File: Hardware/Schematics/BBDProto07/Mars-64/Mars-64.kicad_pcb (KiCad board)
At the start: 4 copper layers, 50.8 x 50.8 mm, 79 parts, among them J101 Conn_Coaxial, J102 Conn_Coaxial, U101 ADG731, U102 ADG731

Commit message: Created the rev D of the schematics
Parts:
- moved U102 72.1 mm to (78.7, 137.2)
- moved C2 71.1 mm to (61.0, 139.7), turned to 0 degrees
- moved J102 68.4 mm to (94.0, 137.2)
- moved JP5 58.8 mm to (61.0, 134.6), turned to 0 degrees
- moved H3 52.4 mm to (58.4, 127.0)
- moved H4 50.6 mm to (99.1, 127.0)
- moved TP109 49.1 mm to (61.0, 88.9)
- moved TP110 49.1 mm to (66.0, 88.9)
- moved TP111 49.1 mm to (71.1, 88.9)
- moved TP112 49.1 mm to (76.2, 88.9)
- moved TP113 49.1 mm to (81.3, 88.9)
- moved TP114 49.1 mm to (86.4, 88.9)
- moved TP115 49.1 mm to (91.4, 88.9)
- moved TP116 49.1 mm to (96.5, 88.9)
- moved TP117 49.1 mm to (61.0, 94.0)
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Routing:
- net GND: track 170.2 -> 0.00 mm, vias 2 -> 0
- net /VCC3V3: track 145.0 -> 0.00 mm
- net Net-(JP5-Pad2): track 112.4 -> 0.00 mm, vias 2 -> 0
- net /~SPI_CE: track 101.9 -> 0.00 mm, vias 3 -> 0
- net Net-(TP207-Pad1): track 74.5 -> 0.00 mm, vias 2 -> 1
- net Net-(J101-Pad2): track 70.3 -> 0.00 mm, vias 2 -> 0
- net Net-(TP217-Pad1): track 65.8 -> 0.00 mm, vias 2 -> 1
- net Net-(TP208-Pad1): track 64.1 -> 0.00 mm, vias 2 -> 1
- net /DB: track 56.3 -> 0.00 mm, vias 2 -> 0
- net Net-(TP123-Pad1): track 55.6 -> 0.00 mm, vias 2 -> 1
- net /DA: track 55.3 -> 0.00 mm, vias 2 -> 0
- net Net-(TP109-Pad1): track 53.6 -> 0.00 mm, vias 2 -> 1
- net Net-(TP111-Pad1): track 51.3 -> 0.00 mm, vias 2 -> 1
- net Net-(TP206-Pad1): track 51.2 -> 0.00 mm, vias 2 -> 1
- net Net-(TP220-Pad1): track 50.3 -> 0.00 mm, vias 2 -> 1
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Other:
- board size 50.8 x 50.8 mm -> 45.7 x 104.1 mm
- board text added: "BBD Mars-64 rev. D"
- board text removed: "BBD Mars-64 rev. C"

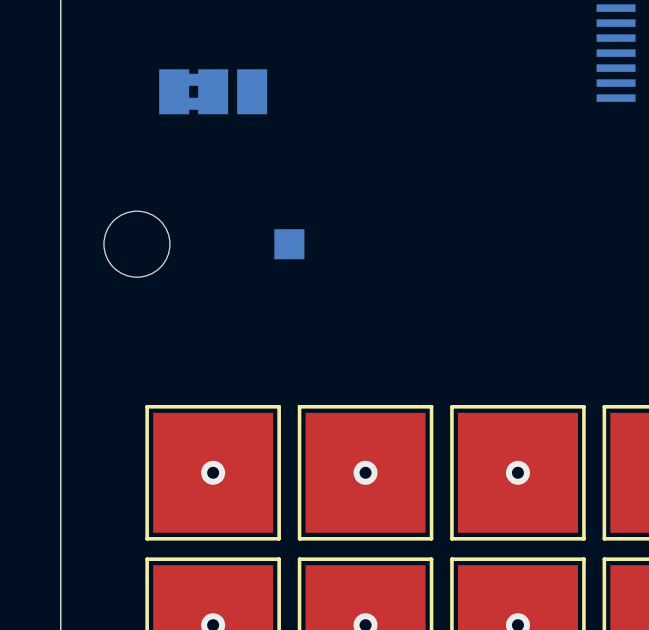
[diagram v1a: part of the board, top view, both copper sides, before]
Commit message: Connected the AGND to the fill zone
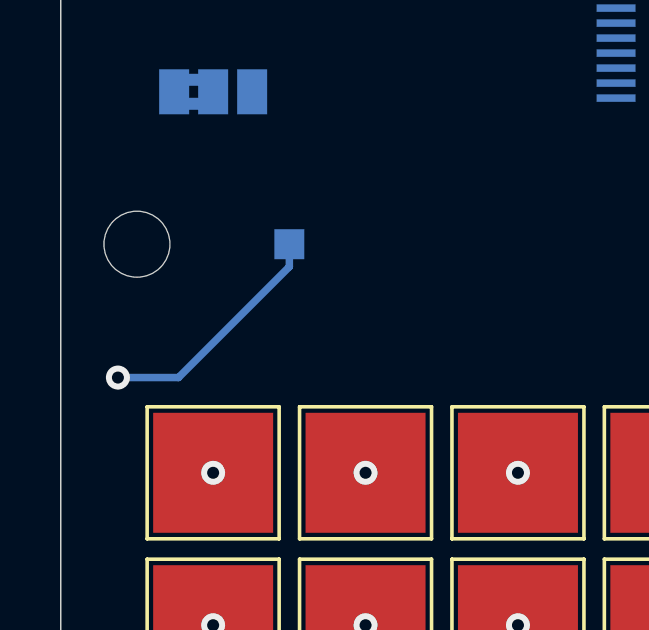
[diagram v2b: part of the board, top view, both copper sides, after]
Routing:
- net /AGND: track 0.00 -> 8.00 mm, vias 0 -> 1
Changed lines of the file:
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@@
     (thickness 1.6)
     (drawings 8)
-    (tracks 64)
+    (tracks 68)
     (zones 0)
     (modules 79)
@@
   (gr_line (start 101.6 144.78) (end 55.88 144.78) (layer Edge.Cuts) (width 0.05))
   (gr_line (start 55.88 40.64) (end 101.6 40.64) (layer Edge.Cuts) (width 0.05))
+  (via (at 57.785 80.645) (size 0.8) (drill 0.4) (layers F.Cu B.Cu) (net 6))
+  (segment (start 63.5 76.95) (end 63.5 76.2) (width 0.25) (layer B.Cu) (net 6))
+  (segment (start 59.805 80.645) (end 63.5 76.95) (width 0.25) (layer B.Cu) (net 6))
+  (segment (start 57.785 80.645) (end 59.805 80.645) (width 0.25) (layer B.Cu) (net 6))
+  (via (at 60.96 83.82) (size 0.8) (drill 0.4) (layers F.Cu B.Cu) (net 9))
+  (via (at 66.04 83.82) (size 0.8) (drill 0.4) (layers F.Cu B.Cu) (net 10))
+  (via (at 71.12 83.82) (size 0.8) (drill 0.4) (layers F.Cu B.Cu) (net 11))
+  (via (at 76.2 83.82) (size 0.8) (drill 0.4) (layers F.Cu B.Cu) (net 12))
+  (via (at 81.28 83.82) (size 0.8) (drill 0.4) (layers F.Cu B.Cu) (net 13))
+  (via (at 86.36 83.82) (size 0.8) (drill 0.4) (layers F.Cu B.Cu) (net 14))
+  (via (at 91.44 83.82) (size 0.8) (drill 0.4) (layers F.Cu B.Cu) (net 15))
+  (via (at 96.52 83.82) (size 0.8) (drill 0.4) (layers F.Cu B.Cu) (net 16))
+  (via (at 60.96 88.9) (size 0.8) (drill 0.4) (layers F.Cu B.Cu) (net 17))
+  (via (at 66.04 88.9) (size 0.8) (drill 0.4) (layers F.Cu B.Cu) (net 18))
+  (via (at 71.12 88.9) (size 0.8) (drill 0.4) (layers F.Cu B.Cu) (net 19))
+  (via (at 76.2 88.9) (size 0.8) (drill 0.4) (layers F.Cu B.Cu) (net 20))
+  (via (at 81.28 88.9) (size 0.8) (drill 0.4) (layers F.Cu B.Cu) (net 21))
+  (via (at 86.36 88.9) (size 0.8) (drill 0.4) (layers F.Cu B.Cu) (net 22))
+  (via (at 91.44 88.9) (size 0.8) (drill 0.4) (layers F.Cu B.Cu) (net 23))
+  (via (at 96.52 88.9) (size 0.8) (drill 0.4) (layers F.Cu B.Cu) (net 24))
+  (via (at 60.96 93.98) (size 0.8) (drill 0.4) (layers F.Cu B.Cu) (net 25))
+  (via (at 66.04 93.98) (size 0.8) (drill 0.4) (layers F.Cu B.Cu) (net 26))
+  (via (at 71.12 93.98) (size 0.8) (drill 0.4) (layers F.Cu B.Cu) (net 27))
+  (via (at 76.2 93.98) (size 0.8) (drill 0.4) (layers F.Cu B.Cu) (net 28))
+  (via (at 81.28 93.98) (size 0.8) (drill 0.4) (layers F.Cu B.Cu) (net 29))
+  (via (at 86.36 93.98) (size 0.8) (drill 0.4) (layers F.Cu B.Cu) (net 30))
+  (via (at 91.44 93.98) (size 0.8) (drill 0.4) (layers F.Cu B.Cu) (net 31))
+  (via (at 96.52 93.98) (size 0.8) (drill 0.4) (layers F.Cu B.Cu) (net 32))
+  (via (at 60.96 99.06) (size 0.8) (drill 0.4) (layers F.Cu B.Cu) (net 33))
+  (via (at 66.04 99.06) (size 0.8) (drill 0.4) (layers F.Cu B.Cu) (net 34))
+  (via (at 71.12 99.06) (size 0.8) (drill 0.4) (layers F.Cu B.Cu) (net 35))
+  (via (at 76.2 99.06) (size 0.8) (drill 0.4) (layers F.Cu B.Cu) (net 36))
+  (via (at 81.28 99.06) (size 0.8) (drill 0.4) (layers F.Cu B.Cu) (net 37))
+  (via (at 86.36 99.06) (size 0.8) (drill 0.4) (layers F.Cu B.Cu) (net 38))
+  (via (at 91.44 99.06) (size 0.8) (drill 0.4) (layers F.Cu B.Cu) (net 39))
+  (via (at 96.52 99.06) (size 0.8) (drill 0.4) (layers F.Cu B.Cu) (net 40))
+  (via (at 60.96 104.14) (size 0.8) (drill 0.4) (layers F.Cu B.Cu) (net 41))
+  (via (at 66.04 104.14) (size 0.8) (drill 0.4) (layers F.Cu B.Cu) (net 42))
+  (via (at 71.12 104.14) (size 0.8) (drill 0.4) (layers F.Cu B.Cu) (net 43))
+  (via (at 76.2 104.14) (size 0.8) (drill 0.4) (layers F.Cu B.Cu) (net 44))
+  (via (at 81.28 104.14) (size 0.8) (drill 0.4) (layers F.Cu B.Cu) (net 45))
+  (via (at 86.36 104.14) (size 0.8) (drill 0.4) (layers F.Cu B.Cu) (net 46))
+  (via (at 91.44 104.14) (size 0.8) (drill 0.4) (layers F.Cu B.Cu) (net 47))
+  (via (at 96.52 104.14) (size 0.8) (drill 0.4) (layers F.Cu B.Cu) (net 48))
+  (via (at 60.96 109.22) (size 0.8) (drill 0.4) (layers F.Cu B.Cu) (net 49))
+  (via (at 66.04 109.22) (size 0.8) (drill 0.4) (layers F.Cu B.Cu) (net 50))
+  (via (at 71.12 109.22) (size 0.8) (drill 0.4) (layers F.Cu B.Cu) (net 51))
+  (via (at 76.2 109.22) (size 0.8) (drill 0.4) (layers F.Cu B.Cu) (net 52))
+  (via (at 81.28 109.22) (size 0.8) (drill 0.4) (layers F.Cu B.Cu) (net 53))
+  (via (at 86.36 109.22) (size 0.8) (drill 0.4) (layers F.Cu B.Cu) (net 54))
+  (via (at 91.44 109.22) (size 0.8) (drill 0.4) (layers F.Cu B.Cu) (net 55))
+  (via (at 96.52 109.22) (size 0.8) (drill 0.4) (layers F.Cu B.Cu) (net 56))
+  (via (at 60.96 114.3) (size 0.8) (drill 0.4) (layers F.Cu B.Cu) (net 57))
+  (via (at 66.04 114.3) (size 0.8) (drill 0.4) (layers F.Cu B.Cu) (net 58))
+  (via (at 71.12 114.3) (size 0.8) (drill 0.4) (layers F.Cu B.Cu) (net 59))
+  (via (at 76.2 114.3) (size 0.8) (drill 0.4) (layers F.Cu B.Cu) (net 60))
+  (via (at 81.28 114.3) (size 0.8) (drill 0.4) (layers F.Cu B.Cu) (net 61))
+  (via (at 86.36 114.3) (size 0.8) (drill 0.4) (layers F.Cu B.Cu) (net 62))
+  (via (at 91.44 114.3) (size 0.8) (drill 0.4) (layers F.Cu B.Cu) (net 63))
+  (via (at 96.52 114.3) (size 0.8) (drill 0.4) (layers F.Cu B.Cu) (net 64))
   (via (at 60.96 119.38) (size 0.8) (drill 0.4) (layers F.Cu B.Cu) (net 65))
   (via (at 66.04 119.38) (size 0.8) (drill 0.4) (layers F.Cu B.Cu) (net 66))
@@
   (via (at 91.44 119.38) (size 0.8) (drill 0.4) (layers F.Cu B.Cu) (net 71))
   (via (at 96.52 119.38) (size 0.8) (drill 0.4) (layers F.Cu B.Cu) (net 72))
-  (via (at 96.52 114.3) (size 0.8) (drill 0.4) (layers F.Cu B.Cu) (net 64))
-  (via (at 91.44 114.3) (size 0.8) (drill 0.4) (layers F.Cu B.Cu) (net 63))
-  (via (at 86.36 114.3) (size 0.8) (drill 0.4) (layers F.Cu B.Cu) (net 62))
-  (via (at 81.28 114.3) (size 0.8) (drill 0.4) (layers F.Cu B.Cu) (net 61))
-  (via (at 76.2 114.3) (size 0.8) (drill 0.4) (layers F.Cu B.Cu) (net 60))
-  (via (at 71.12 114.3) (size 0.8) (drill 0.4) (layers F.Cu B.Cu) (net 59))
-  (via (at 66.04 114.3) (size 0.8) (drill 0.4) (layers F.Cu B.Cu) (net 58))
-  (via (at 60.96 114.3) (size 0.8) (drill 0.4) (layers F.Cu B.Cu) (net 57))
-  (via (at 60.96 109.22) (size 0.8) (drill 0.4) (layers F.Cu B.Cu) (net 49))
-  (via (at 66.04 109.22) (size 0.8) (drill 0.4) (layers F.Cu B.Cu) (net 50))
-  (via (at 71.12 109.22) (size 0.8) (drill 0.4) (layers F.Cu B.Cu) (net 51))
-  (via (at 76.2 109.22) (size 0.8) (drill 0.4) (layers F.Cu B.Cu) (net 52))
-  (via (at 81.28 109.22) (size 0.8) (drill 0.4) (layers F.Cu B.Cu) (net 53))
-  (via (at 86.36 109.22) (size 0.8) (drill 0.4) (layers F.Cu B.Cu) (net 54))
-  (via (at 91.44 109.22) (size 0.8) (drill 0.4) (layers F.Cu B.Cu) (net 55))
-  (via (at 96.52 109.22) (size 0.8) (drill 0.4) (layers F.Cu B.Cu) (net 56))
-  (via (at 96.52 104.14) (size 0.8) (drill 0.4) (layers F.Cu B.Cu) (net 48))
-  (via (at 91.44 104.14) (size 0.8) (drill 0.4) (layers F.Cu B.Cu) (net 47))
-  (via (at 86.36 104.14) (size 0.8) (drill 0.4) (layers F.Cu B.Cu) (net 46))
-  (via (at 81.28 104.14) (size 0.8) (drill 0.4) (layers F.Cu B.Cu) (net 45))
-  (via (at 76.2 104.14) (size 0.8) (drill 0.4) (layers F.Cu B.Cu) (net 44))
-  (via (at 71.12 104.14) (size 0.8) (drill 0.4) (layers F.Cu B.Cu) (net 43))
-  (via (at 66.04 104.14) (size 0.8) (drill 0.4) (layers F.Cu B.Cu) (net 42))
-  (via (at 60.96 104.14) (size 0.8) (drill 0.4) (layers F.Cu B.Cu) (net 41))
-  (via (at 60.96 93.98) (size 0.8) (drill 0.4) (layers F.Cu B.Cu) (net 25))
-  (via (at 60.96 99.06) (size 0.8) (drill 0.4) (layers F.Cu B.Cu) (net 33))
-  (via (at 66.04 99.06) (size 0.8) (drill 0.4) (layers F.Cu B.Cu) (net 34))
-  (via (at 66.04 93.98) (size 0.8) (drill 0.4) (layers F.Cu B.Cu) (net 26))
-  (via (at 96.52 99.06) (size 0.8) (drill 0.4) (layers F.Cu B.Cu) (net 40))
-  (via (at 91.44 99.06) (size 0.8) (drill 0.4) (layers F.Cu B.Cu) (net 39))
-  (via (at 86.36 99.06) (size 0.8) (drill 0.4) (layers F.Cu B.Cu) (net 38))
-  (via (at 81.28 99.06) (size 0.8) (drill 0.4) (layers F.Cu B.Cu) (net 37))
-  (via (at 76.2 99.06) (size 0.8) (drill 0.4) (layers F.Cu B.Cu) (net 36))
-  (via (at 71.12 99.06) (size 0.8) (drill 0.4) (layers F.Cu B.Cu) (net 35))
-  (via (at 71.12 93.98) (size 0.8) (drill 0.4) (layers F.Cu B.Cu) (net 27))
-  (via (at 76.2 93.98) (size 0.8) (drill 0.4) (layers F.Cu B.Cu) (net 28))
-  (via (at 81.28 93.98) (size 0.8) (drill 0.4) (layers F.Cu B.Cu) (net 29))
-  (via (at 96.52 93.98) (size 0.8) (drill 0.4) (layers F.Cu B.Cu) (net 32))
-  (via (at 91.44 93.98) (size 0.8) (drill 0.4) (layers F.Cu B.Cu) (net 31))
-  (via (at 86.36 93.98) (size 0.8) (drill 0.4) (layers F.Cu B.Cu) (net 30))
-  (via (at 86.36 88.9) (size 0.8) (drill 0.4) (layers F.Cu B.Cu) (net 22))
-  (via (at 91.44 88.9) (size 0.8) (drill 0.4) (layers F.Cu B.Cu) (net 23))
-  (via (at 96.52 88.9) (size 0.8) (drill 0.4) (layers F.Cu B.Cu) (net 24))
-  (via (at 96.52 83.82) (size 0.8) (drill 0.4) (layers F.Cu B.Cu) (net 16))
-  (via (at 91.44 83.82) (size 0.8) (drill 0.4) (layers F.Cu B.Cu) (net 15))
-  (via (at 86.36 83.82) (size 0.8) (drill 0.4) (layers F.Cu B.Cu) (net 14))
-  (via (at 60.96 88.9) (size 0.8) (drill 0.4) (layers F.Cu B.Cu) (net 17))
-  (via (at 66.04 88.9) (size 0.8) (drill 0.4) (layers F.Cu B.Cu) (net 18))
-  (via (at 71.12 88.9) (size 0.8) (drill 0.4) (layers F.Cu B.Cu) (net 19))
-  (via (at 76.2 88.9) (size 0.8) (drill 0.4) (layers F.Cu B.Cu) (net 20))
-  (via (at 81.28 88.9) (size 0.8) (drill 0.4) (layers F.Cu B.Cu) (net 21))
-  (via (at 81.28 83.82) (size 0.8) (drill 0.4) (layers F.Cu B.Cu) (net 13))
-  (via (at 76.2 83.82) (size 0.8) (drill 0.4) (layers F.Cu B.Cu) (net 12))
-  (via (at 71.12 83.82) (size 0.8) (drill 0.4) (layers F.Cu B.Cu) (net 11))
-  (via (at 66.04 83.82) (size 0.8) (drill 0.4) (layers F.Cu B.Cu) (net 10))
-  (via (at 60.96 83.82) (size 0.8) (drill 0.4) (layers F.Cu B.Cu) (net 9))
   (zone (net 6) (net_name /AGND) (layer In1.Cu) (hatch edge 0.508)
     (connect_pads yes (clearance 0.508))

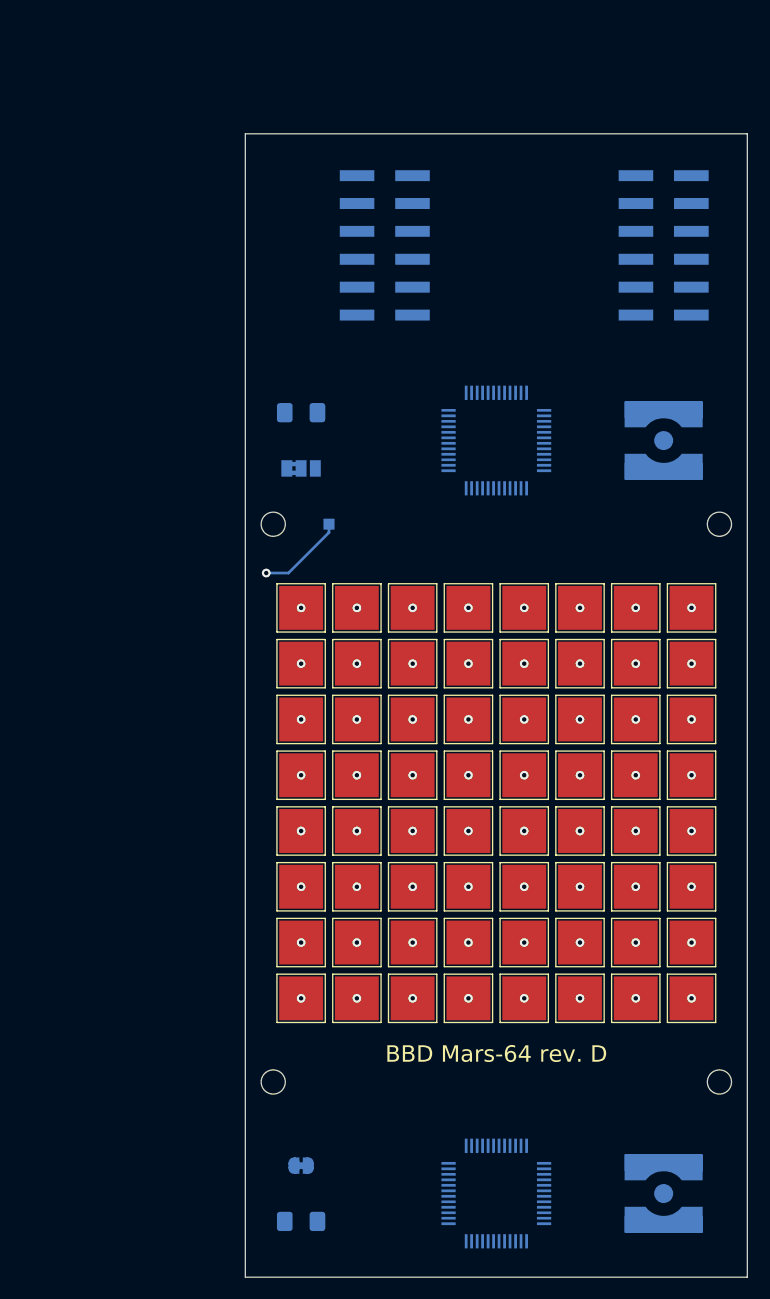
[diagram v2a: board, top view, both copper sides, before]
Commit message: Made the board smaller
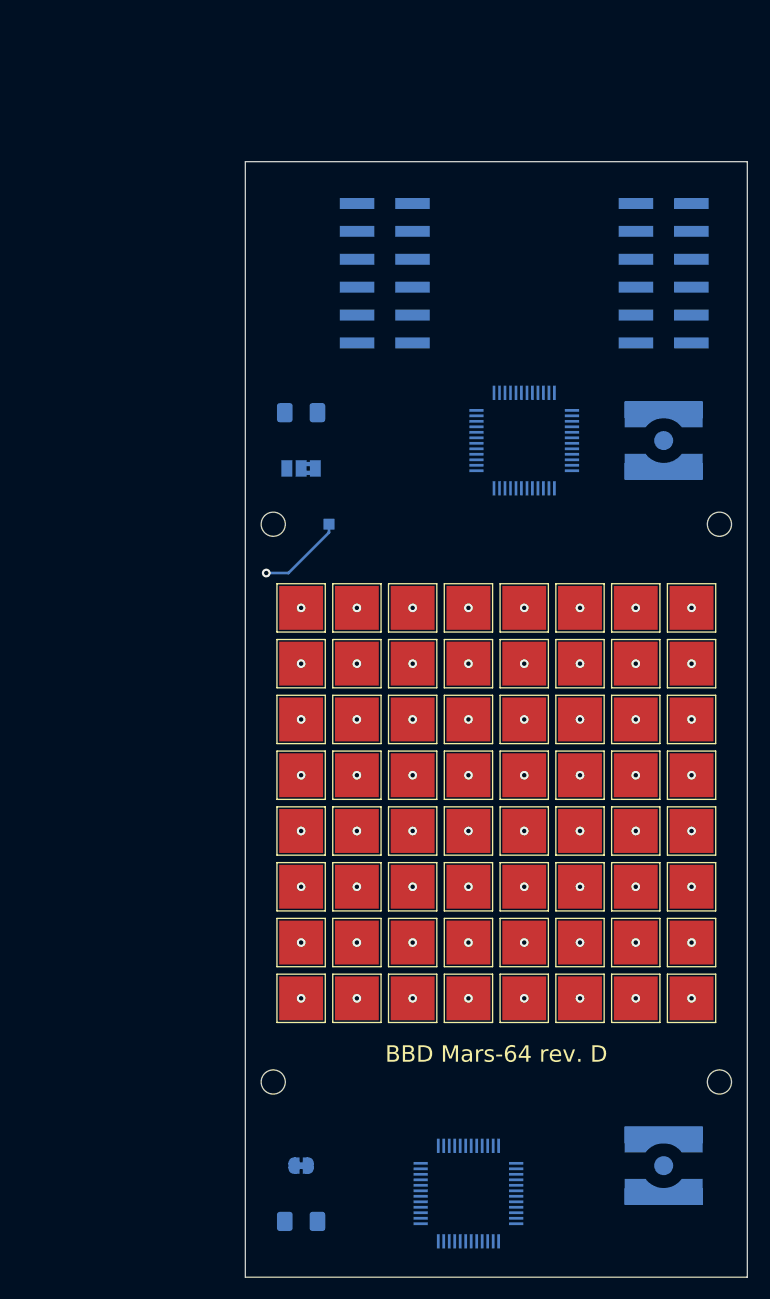
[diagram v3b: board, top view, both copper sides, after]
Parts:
- moved PmodF2 2.54 mm to (68.6, 53.3)
- moved PmodM1 2.54 mm to (94.0, 53.3)
- moved U101 2.54 mm to (81.3, 68.6)
- moved J102 2.54 mm to (94.0, 134.6)
- moved U102 2.54 mm to (76.2, 137.2)
- turned JP4 to 180 degrees
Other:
- board size 45.7 x 104.1 mm -> 45.7 x 101.6 mm
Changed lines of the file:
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@@
   )
   (module Connector_Coaxial:SMA_Amphenol_132134-10_Vertical (layer B.Cu)
-    (at 93.98 137.16)
+    (at 93.98 134.62)
     (descr https://www.amphenolrf.com/downloads/dl/file/id/4007/product/2974/132134_10_customer_drawing.pdf)
     (tags "SMA SMD Female Jack Vertical")
@@
   )
   (module Jumper:SolderJumper-3_P1.3mm_Bridged2Bar12_Pad1.0x1.5mm_NumberLabels (layer B.Cu)
-    (at 60.96 71.12)
+    (at 60.96 71.12 180)
     (descr "SMD Solder Jumper, 1x1.5mm Pads, 0.3mm gap, pads 1-2 Bridged2Bar with 2 copper strip, labeled with numbers")
     (tags "solder jumper open")
@@
     (fp_poly (pts (xy -0.9 -0.2) (xy -0.4 -0.2) (xy -0.4 -0.6) (xy -0.9 -0.6)) (layer B.Cu) (width 0))
     (fp_poly (pts (xy -0.9 0.6) (xy -0.4 0.6) (xy -0.4 0.2) (xy -0.9 0.2)) (layer B.Cu) (width 0))
-    (pad 1 smd rect (at -1.3 0) (size 1 1.5) (layers B.Cu B.Mask)
+    (pad 1 smd rect (at -1.3 0 180) (size 1 1.5) (layers B.Cu B.Mask)
       (net 6 /AGND))
-    (pad 3 smd rect (at 1.3 0) (size 1 1.5) (layers B.Cu B.Mask)
-      (net 4 GND))
-    (pad 2 smd rect (at 0 0) (size 1 1.5) (layers B.Cu B.Mask)
+    (pad 3 smd rect (at 1.3 0 180) (size 1 1.5) (layers B.Cu B.Mask)
+      (net 4 GND))
+    (pad 2 smd rect (at 0 0 180) (size 1 1.5) (layers B.Cu B.Mask)
       (net 73 "Net-(J101-Pad2)"))
   )
   (module Mars-64:PinHeader_2x06_P2.54mm_Vertical_SMD_TopBottom (layer B.Cu)
-    (at 93.98 50.8)
+    (at 93.98 53.34)
     (descr "surface-mounted straight pin header, 2x06, 2.54mm pitch, double rows")
     (tags "Surface mounted pin header SMD 2x06 2.54mm double row")
@@
   )
   (module Mars-64:PinHeader_2x06_P2.54mm_Vertical_SMD_TopBottom_Mirrored (layer B.Cu)
-    (at 68.58 50.8)
+    (at 68.58 53.34)
     (descr "surface-mounted straight pin header, 2x06, 2.54mm pitch, double rows")
     (tags "Surface mounted pin header SMD 2x06 2.54mm double row")
@@
   )
   (module Package_QFP:TQFP-48_7x7mm_P0.5mm (layer B.Cu)
-    (at 78.74 68.58 180)
+    (at 81.28 68.58 180)
     (descr "48 LEAD TQFP 7x7mm (see MICREL TQFP7x7-48LD-PL-1.pdf)")
     (tags "QFP 0.5")
@@
   )
   (module Package_QFP:TQFP-48_7x7mm_P0.5mm (layer B.Cu)
-    (at 78.74 137.16)
+    (at 76.2 137.16)
     (descr "48 LEAD TQFP 7x7mm (see MICREL TQFP7x7-48LD-PL-1.pdf)")
     (tags "QFP 0.5")
@@
     )
   )
-  (dimension 104.14 (width 0.15) (layer Dwgs.User)
-    (gr_text "104.140 mm" (at 107.98 92.71 270) (layer Dwgs.User)
+  (dimension 101.6 (width 0.15) (layer Dwgs.User)
+    (gr_text "101.600 mm" (at 107.98 93.98 270) (layer Dwgs.User)
       (effects (font (size 1 1) (thickness 0.15)))
     )
     (feature1 (pts (xy 101.6 144.78) (xy 107.266421 144.78)))
-    (feature2 (pts (xy 101.6 40.64) (xy 107.266421 40.64)))
-    (crossbar (pts (xy 106.68 40.64) (xy 106.68 144.78)))
+    (feature2 (pts (xy 101.6 43.18) (xy 107.266421 43.18)))
+    (crossbar (pts (xy 106.68 43.18) (xy 106.68 144.78)))
     (arrow1a (pts (xy 106.68 144.78) (xy 106.093579 143.653496)))
     (arrow1b (pts (xy 106.68 144.78) (xy 107.266421 143.653496)))
-    (arrow2a (pts (xy 106.68 40.64) (xy 106.093579 41.766504)))
-    (arrow2b (pts (xy 106.68 40.64) (xy 107.266421 41.766504)))
+    (arrow2a (pts (xy 106.68 43.18) (xy 106.093579 44.306504)))
+    (arrow2b (pts (xy 106.68 43.18) (xy 107.266421 44.306504)))
   )
   (dimension 45.72 (width 0.15) (layer Dwgs.User)
-    (gr_text "45.720 mm" (at 78.74 34.26) (layer Dwgs.User)
+    (gr_text "45.720 mm" (at 78.74 36.8) (layer Dwgs.User)
       (effects (font (size 1 1) (thickness 0.15)))
     )
-    (feature1 (pts (xy 101.6 40.64) (xy 101.6 34.973579)))
-    (feature2 (pts (xy 55.88 40.64) (xy 55.88 34.973579)))
-    (crossbar (pts (xy 55.88 35.56) (xy 101.6 35.56)))
-    (arrow1a (pts (xy 101.6 35.56) (xy 100.473496 36.146421)))
-    (arrow1b (pts (xy 101.6 35.56) (xy 100.473496 34.973579)))
-    (arrow2a (pts (xy 55.88 35.56) (xy 57.006504 36.146421)))
-    (arrow2b (pts (xy 55.88 35.56) (xy 57.006504 34.973579)))
+    (feature1 (pts (xy 101.6 43.18) (xy 101.6 37.513579)))
+    (feature2 (pts (xy 55.88 43.18) (xy 55.88 37.513579)))
+    (crossbar (pts (xy 55.88 38.1) (xy 101.6 38.1)))
+    (arrow1a (pts (xy 101.6 38.1) (xy 100.473496 38.686421)))
+    (arrow1b (pts (xy 101.6 38.1) (xy 100.473496 37.513579)))
+    (arrow2a (pts (xy 55.88 38.1) (xy 57.006504 38.686421)))
+    (arrow2b (pts (xy 55.88 38.1) (xy 57.006504 37.513579)))
   )
   (gr_text "BBD Mars-64 rev. D" (at 78.74 124.46) (layer F.SilkS)
@@
     (effects (font (size 1.5 1.5) (thickness 0.3)) (justify mirror))
   )
-  (gr_line (start 55.88 40.64) (end 55.88 144.78) (layer Edge.Cuts) (width 0.05))
-  (gr_line (start 101.6 40.64) (end 101.6 144.78) (layer Edge.Cuts) (width 0.05))
+  (gr_line (start 55.88 43.18) (end 55.88 144.78) (layer Edge.Cuts) (width 0.05))
+  (gr_line (start 101.6 43.18) (end 101.6 144.78) (layer Edge.Cuts) (width 0.05))
   (gr_line (start 101.6 144.78) (end 55.88 144.78) (layer Edge.Cuts) (width 0.05))
-  (gr_line (start 55.88 40.64) (end 101.6 40.64) (layer Edge.Cuts) (width 0.05))
+  (gr_line (start 55.88 43.18) (end 101.6 43.18) (layer Edge.Cuts) (width 0.05))
   (via (at 57.785 80.645) (size 0.8) (drill 0.4) (layers F.Cu B.Cu) (net 6))
   (segment (start 63.5 76.95) (end 63.5 76.2) (width 0.25) (layer B.Cu) (net 6))
